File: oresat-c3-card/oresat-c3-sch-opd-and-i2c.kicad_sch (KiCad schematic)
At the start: 38 parts, among them Q1 NTR4101P, U12 RCLAMP0504FB, U13 MAX892LEUA+T, U24 RV-3028-C7, U30 FM24CL64B-GTR, U37 LTC4300A-1

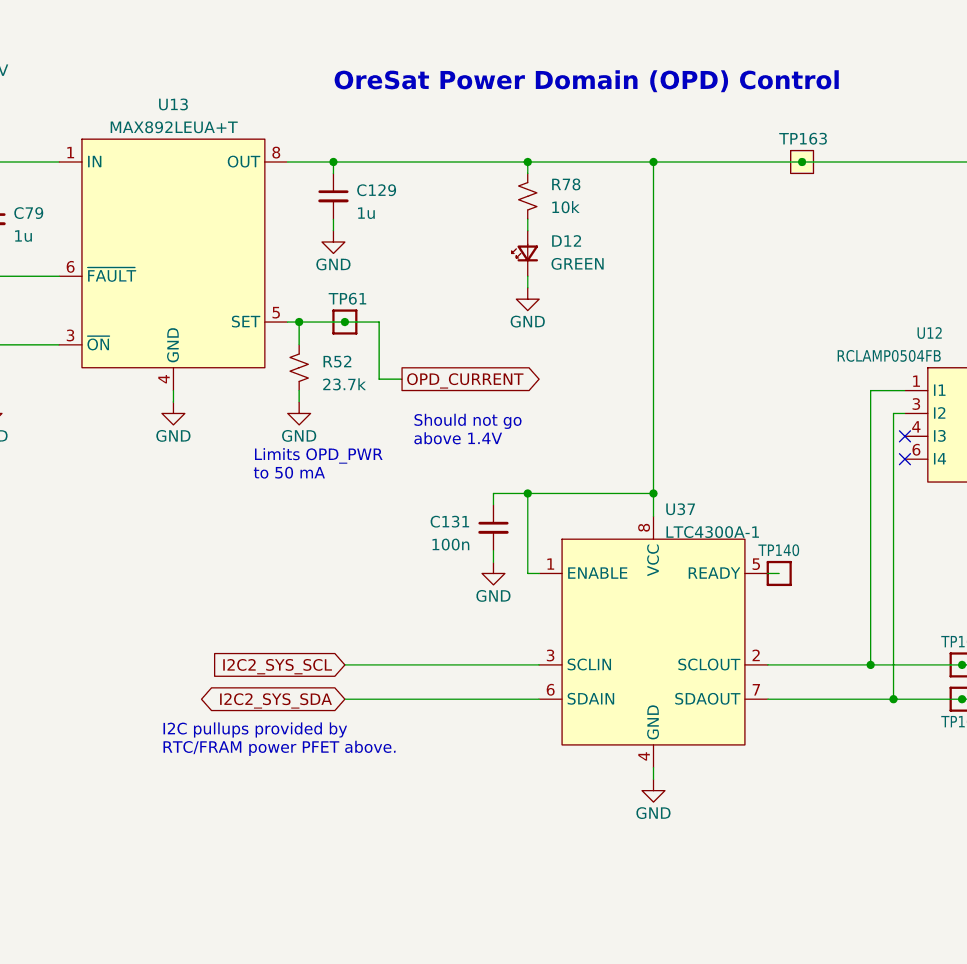
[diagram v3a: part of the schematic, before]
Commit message: Design review on C3 v7.0
Glenn and Andrew did a design review. Removed fiducials on back of board. Lots of schematic fixes, including
direction connection of TCXOs to AT86s, corrected LPF of CLKO from AT86 to the synth reference, fixed drive
levels both QPC switches in UHF radio, confirmed QPC directions, and some minor polishing.
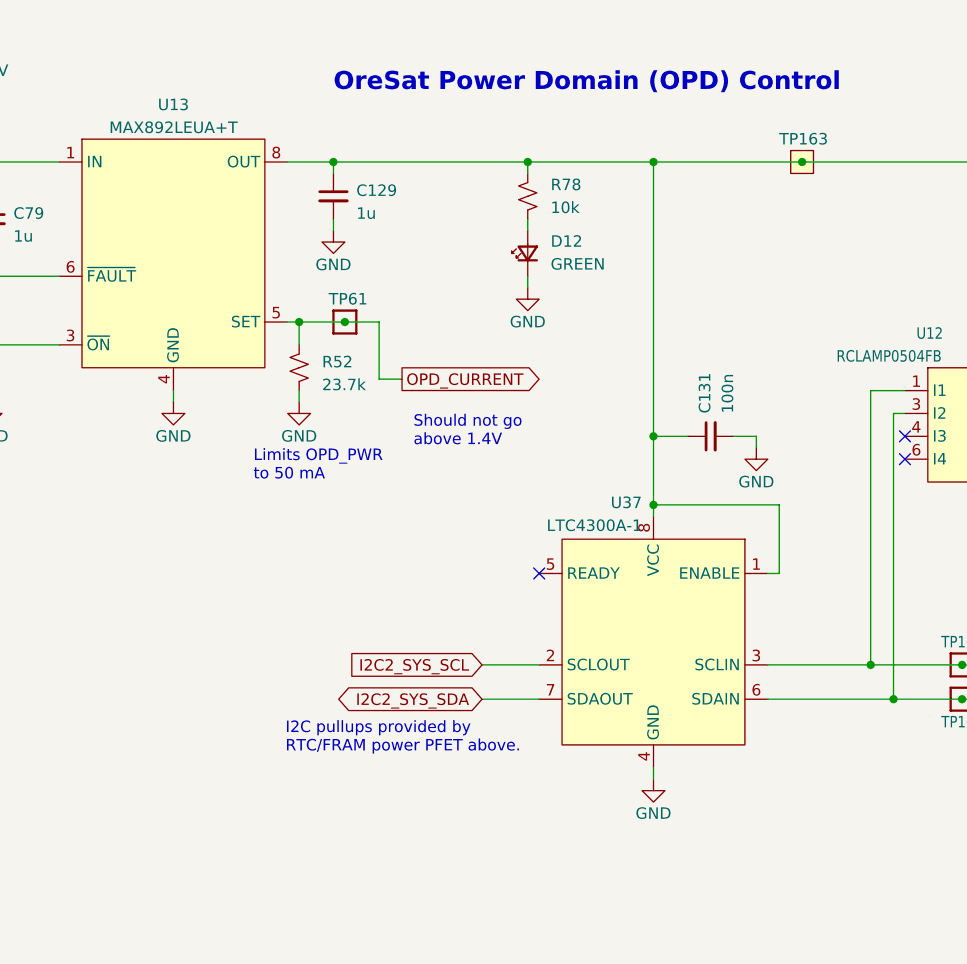
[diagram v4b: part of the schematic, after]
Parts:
- removed TP140: Test-Point, oresat-misc:TestPoint_Pad_D1.0mm, symbol oresat-misc:Test-Point-1mm-round
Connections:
- net I2C2_SYS_SCL: now also U37.2 (SCLOUT); no longer U37.3 (SCLIN)
- net I2C2_SYS_SDA: now also U37.7 (SDAOUT); no longer U37.6 (SDAIN)
- net OPD_SCL: now also U37.3 (SCLIN); no longer U37.2 (SCLOUT)
- net OPD_SDA: now also U37.6 (SDAIN); no longer U37.7 (SDAOUT)
- no-connect marks 2 -> 3
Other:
- moved on the sheet: C131

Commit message: Updated footprints to latest KiCad; optimize L band AT86 placement, cleanup UHF AT86 connections
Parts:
- U24: footprint oresat-c3-eagle-import:RV3028C732768KHZ1PPMTAQC -> Package_SON:MicroCrystal_C7_SON-8_1.5x3.2mm_P0.9mm
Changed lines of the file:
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@@
 			)
 		)
-		(property "Footprint" "oresat-c3-eagle-import:RV3028C732768KHZ1PPMTAQC"
+		(property "Footprint" "Package_SON:MicroCrystal_C7_SON-8_1.5x3.2mm_P0.9mm"
 			(at 181.61 77.47 0)
 			(effects

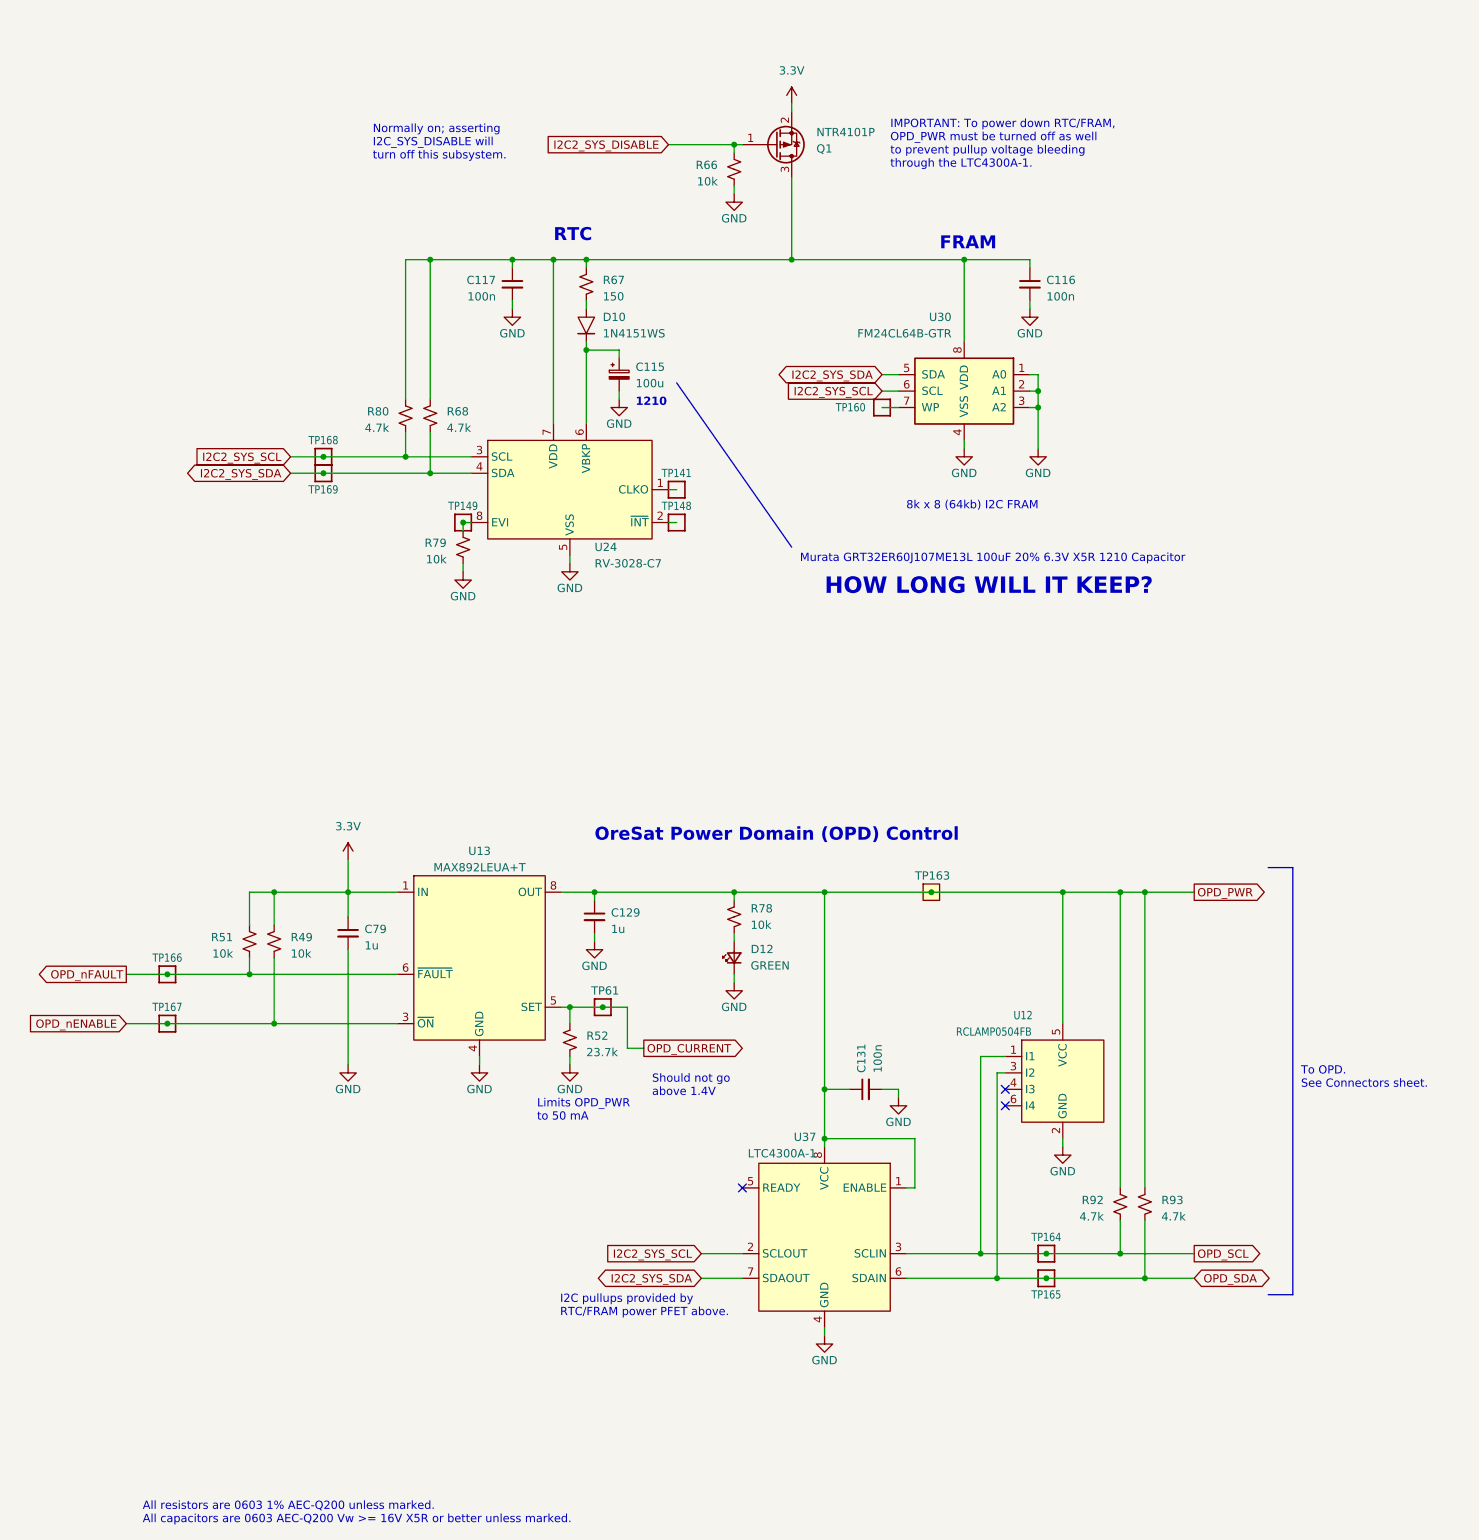
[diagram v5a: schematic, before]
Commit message: Updating BOM and switching to oresat-passive footprints. Fixed some power cutoff limits, and fixed another DC voltage leverl on an LNA!
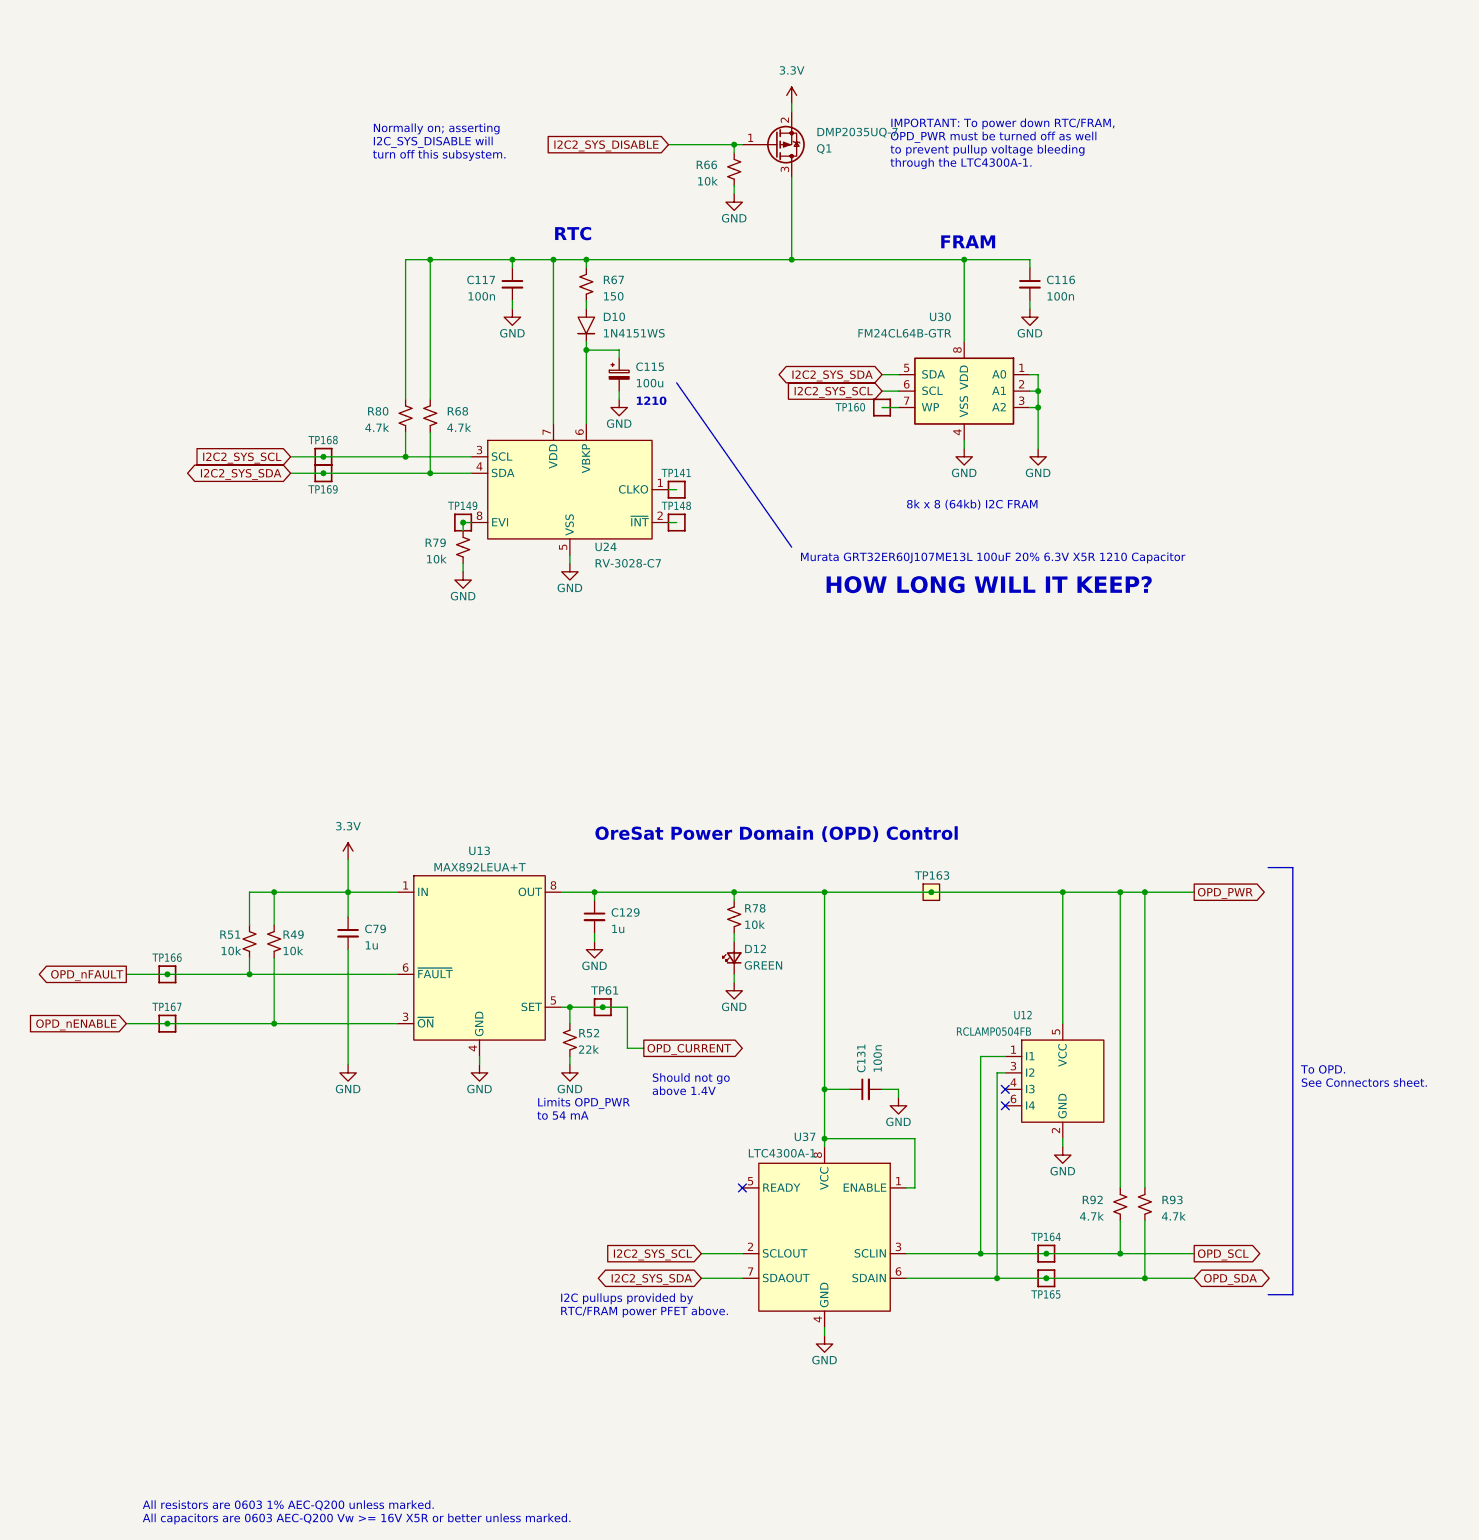
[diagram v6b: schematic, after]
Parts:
- C116, C117, C129, C131, C79, D10, D12, U12, U13, U24, U30: DST Digi-Key -> DigiKey
- Q1: value NTR4101P -> DMP2035UQ-7; DPN NTR4101PT1GOSCT-ND -> 31-DMP2035UQ-7CT-ND; DST Digi-Key -> DigiKey; MFR On Semiconductor -> Diodes Incorporated; MPN NTR4101PT1G -> DMP2035UQ-7
- R49, R51, R66, R78, R79: footprint Resistor_SMD:R_0603_1608Metric -> oresat-passives:0603-C-NOSILK; DST Digi-Key -> DigiKey; MFR Stackpole Electronics Inc -> Stackpole Electronics
- R52: value 23.7k -> 22k; footprint Resistor_SMD:R_0603_1608Metric -> oresat-passives:0603-C-NOSILK; DPN RMCF0603FT23K7CT-ND -> RMCF0603FT22K0CT-ND; DST Digi-Key -> DigiKey; MPN RMCF0603FT23K7 -> RMCF0603FT22K0
- R67, R68, R80, R92, R93: footprint Resistor_SMD:R_0603_1608Metric -> oresat-passives:0603-C-NOSILK; DST Digi-Key -> DigiKey
- U37: DST Digi-Key -> DigiKey; MFR ADI -> Analog Devices
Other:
- note added: "Limits OPD_PWR to 54 mA"
- note removed: "Limits OPD_PWR to 50 mA"

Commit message: All footprints updated. Passes ERC/DRC.
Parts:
- C116, C117, C131: footprint Capacitor_SMD:C_0603_1608Metric -> oresat-passives:0603-C-NOSILK; DPN 587-3472-1-ND -> 399-6856-1-ND; MFR Taiyo Yuden -> KEMET; MPN TMK107BJ104KAHT -> C0603C104K5RACAUTO
- C129, C79: footprint Capacitor_SMD:C_0603_1608Metric -> oresat-passives:0603-C-NOSILK; DPN 587-3473-1-ND -> 490-GRT188R71E105KE13DCT-ND; MFR Taiyo Yuden -> Murata Electronics; MPN TMK107BJ105KAHT -> GRT188R71E105KE13D
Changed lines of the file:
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@@
 			)
 		)
-		(property "Footprint" "Capacitor_SMD:C_0603_1608Metric"
+		(property "Footprint" "oresat-passives:0603-C-NOSILK"
 			(at 252.73 69.85 0)
 			(effects
@@
 			)
 		)
-		(property "Datasheet" "~"
+		(property "Datasheet" "https://search.kemet.com/download/specsheet/C0603C104K5RACAUTO"
 			(at 252.73 69.85 0)
 			(effects
@@
 			)
 		)
-		(property "Description" "100 nF (0.1µF) ±10% 25V Ceramic Capacitor X5R 0603 (1608 Metric)"
+		(property "Description" "0.1 µF ±10% 50V Ceramic Capacitor X7R 0603 (1608 Metric)"
 			(at 252.73 69.85 0)
 			(effects
@@
 			)
 		)
-		(property "DPN" "587-3472-1-ND"
+		(property "DPN" "399-6856-1-ND"
 			(at 252.73 69.85 0)
 			(effects
@@
 			)
 		)
-		(property "MFR" "Taiyo Yuden"
+		(property "MFR" "KEMET"
 			(at 252.73 69.85 0)
 			(effects
@@
 			)
 		)
-		(property "MPN" "TMK107BJ104KAHT"
+		(property "MPN" "C0603C104K5RACAUTO"
 			(at 252.73 69.85 0)
 			(effects
@@
 			)
 		)
-		(property "Footprint" "Capacitor_SMD:C_0603_1608Metric"
+		(property "Footprint" "oresat-passives:0603-C-NOSILK"
 			(at 227.33 194.31 0)
 			(effects
@@
 			)
 		)
-		(property "Datasheet" "~"
+		(property "Datasheet" "https://search.kemet.com/download/specsheet/C0603C104K5RACAUTO"
 			(at 227.33 194.31 0)
 			(effects
@@
 			)
 		)
-		(property "Description" "100 nF (0.1µF) ±10% 25V Ceramic Capacitor X5R 0603 (1608 Metric)"
+		(property "Description" "0.1 µF ±10% 50V Ceramic Capacitor X7R 0603 (1608 Metric)"
 			(at 227.33 194.31 0)
 			(effects
@@
 			)
 		)
-		(property "DPN" "587-3472-1-ND"
+		(property "DPN" "399-6856-1-ND"
 			(at 227.33 194.31 0)
 			(effects
@@
 			)
 		)
-		(property "MFR" "Taiyo Yuden"
+		(property "MFR" "KEMET"
 			(at 227.33 194.31 0)
 			(effects
@@
 			)
 		)
-		(property "MPN" "TMK107BJ104KAHT"
+		(property "MPN" "C0603C104K5RACAUTO"
 			(at 227.33 194.31 0)
 			(effects
@@
 			)
 		)
-		(property "Footprint" "Capacitor_SMD:C_0603_1608Metric"
+		(property "Footprint" "oresat-passives:0603-C-NOSILK"
 			(at 172.72 69.85 0)
 			(effects
@@
 			)
 		)
-		(property "Datasheet" "~"
+		(property "Datasheet" "https://search.kemet.com/download/specsheet/C0603C104K5RACAUTO"
 			(at 172.72 69.85 0)
 			(effects
@@
 			)
 		)
-		(property "Description" "100 nF (0.1µF) ±10% 25V Ceramic Capacitor X5R 0603 (1608 Metric)"
+		(property "Description" "0.1 µF ±10% 50V Ceramic Capacitor X7R 0603 (1608 Metric)"
 			(at 172.72 69.85 0)
 			(effects
@@
 			)
 		)
-		(property "DPN" "587-3472-1-ND"
+		(property "DPN" "399-6856-1-ND"
 			(at 172.72 69.85 0)
 			(effects
@@
 			)
 		)
-		(property "MFR" "Taiyo Yuden"
+		(property "MFR" "KEMET"
 			(at 172.72 69.85 0)
 			(effects
@@
 			)
 		)
-		(property "MPN" "TMK107BJ104KAHT"
+		(property "MPN" "C0603C104K5RACAUTO"
 			(at 172.72 69.85 0)
 			(effects
@@
 			)
 		)
-		(property "Footprint" "Capacitor_SMD:C_0603_1608Metric"
+		(property "Footprint" "oresat-passives:0603-C-NOSILK"
 			(at 185.42 167.64 0)
 			(effects
@@
 			)
 		)
-		(property "Datasheet" "~"
+		(property "Datasheet" "https://search.murata.co.jp/Ceramy/image/img/A01X/G101/ENG/GRT188R71E105KE13-01.pdf"
 			(at 185.42 167.64 0)
 			(effects
@@
 			)
 		)
-		(property "Description" "1µF ±10% 25V Ceramic Capacitor X5R 0603 (1608 Metric)"
+		(property "Description" "1 µF ±10% 25V Ceramic Capacitor X7R 0603 (1608 Metric)"
 			(at 185.42 167.64 0)
 			(effects
@@
 			)
 		)
-		(property "DPN" "587-3473-1-ND"
+		(property "DPN" "490-GRT188R71E105KE13DCT-ND"
 			(at 185.42 167.64 0)
 			(effects
@@
 			)
 		)
-		(property "MFR" "Taiyo Yuden"
+		(property "MFR" "Murata Electronics"
 			(at 185.42 167.64 0)
 			(effects
@@
 			)
 		)
-		(property "MPN" "TMK107BJ105KAHT"
+		(property "MPN" "GRT188R71E105KE13D"
 			(at 185.42 167.64 0)
 			(effects
@@
 			)
 		)
-		(property "Footprint" "Capacitor_SMD:C_0603_1608Metric"
+		(property "Footprint" "oresat-passives:0603-C-NOSILK"
 			(at 147.32 170.18 0)
 			(effects
@@
 			)
 		)
-		(property "Datasheet" "~"
+		(property "Datasheet" "https://search.murata.co.jp/Ceramy/image/img/A01X/G101/ENG/GRT188R71E105KE13-01.pdf"
 			(at 147.32 170.18 0)
 			(effects
@@
 			)
 		)
-		(property "Description" "1µF ±10% 25V Ceramic Capacitor X5R 0603 (1608 Metric)"
+		(property "Description" "1 µF ±10% 25V Ceramic Capacitor X7R 0603 (1608 Metric)"
 			(at 147.32 170.18 0)
 			(effects
@@
 			)
 		)
-		(property "DPN" "587-3473-1-ND"
+		(property "DPN" "490-GRT188R71E105KE13DCT-ND"
 			(at 147.32 170.18 0)
 			(effects
@@
 			)
 		)
-		(property "MFR" "Taiyo Yuden"
+		(property "MFR" "Murata Electronics"
 			(at 147.32 170.18 0)
 			(effects
@@
 			)
 		)
-		(property "MPN" "TMK107BJ105KAHT"
+		(property "MPN" "GRT188R71E105KE13D"
 			(at 147.32 170.18 0)
 			(effects
